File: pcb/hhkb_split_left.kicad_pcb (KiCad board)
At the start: 4 copper layers, 140.4 x 97.4 mm, 67 parts, among them SW1 Esc, SW10 E, SW11 R, SW12 T, SW13 Ctrl, SW14 A, SW15 S, SW16 D, SW17 F, SW18 G, SW19 Shift, SW2 1, SW20 Z, SW21 X, SW22 C, SW23 V, SW24 B, SW25 Alt, SW26 Meta, SW27 L-Space, SW3 2, SW4 3, SW5 4, SW6 5, SW7 Tab, SW8 Q, SW9 W, U1 74HC595

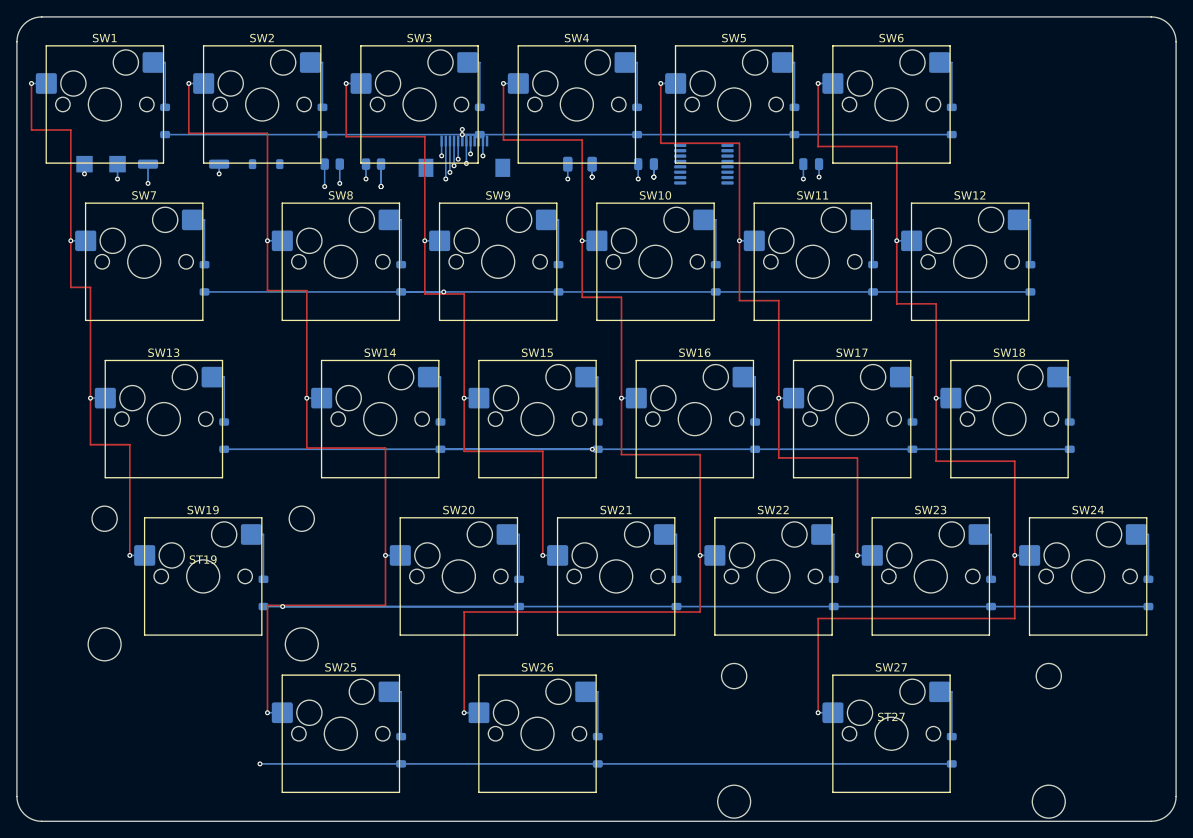
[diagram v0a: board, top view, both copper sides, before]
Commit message: 本体基板の配線が通った（3 基板すべて DRC 違反 0・未配線 0）
Freerouting が詰まっていた原因は 3 つあり、すべて実験で特定した。

1. J_DB（FFC）がダイオード列に載っていた。上段キーのダイオードは帯へ
   1.75mm 食い込み 19.05mm ピッチで並ぶ。帯の部品で J_DB だけ背が高く
   （7.9mm）、その x がちょうど D3 の列だった。短絡・コートヤード重なり・
   ROW0 の未配線はすべてこれが原因。J_DB とその玉突きで C_BULK / C_MCU を
   ダイオードの隙間へ移した

2. GND パッドがベタに届かなかった。GND ベタは In1.Cu の 1 層だけ、GND
   パッドは全部 B.Cu の SMD。間のビアを Freerouting 任せにすると、混んだ
   区画でファンアウトに失敗する（対応 SMD ピンの 42% しか成功しなかった）。
   tools/gnd_fanout.py で配置段階に決定的に立てる

3. ピンが空の (net GND) を DSN に残すと Freerouting が NPE で落ちる。
   GND はネット定義・クラス・plane をまとめて消す。ファンアウトの配線材は
   (type protect) にしてネット無しの固定障害物として渡す（消すと避けない）

ImportSpecctraSES は既存配線を作り直すのでファンアウトが消える
（実測 7 個 → 0 個）。取り込み後に立て直している。

WIP_BOARDS が空になった。DRC の検査が skip ではなく PASS で通る。
検査 249 件通過、組み立て干渉 0。

Co-Authored-By: Claude Opus 5 <noreply@anthropic.com>
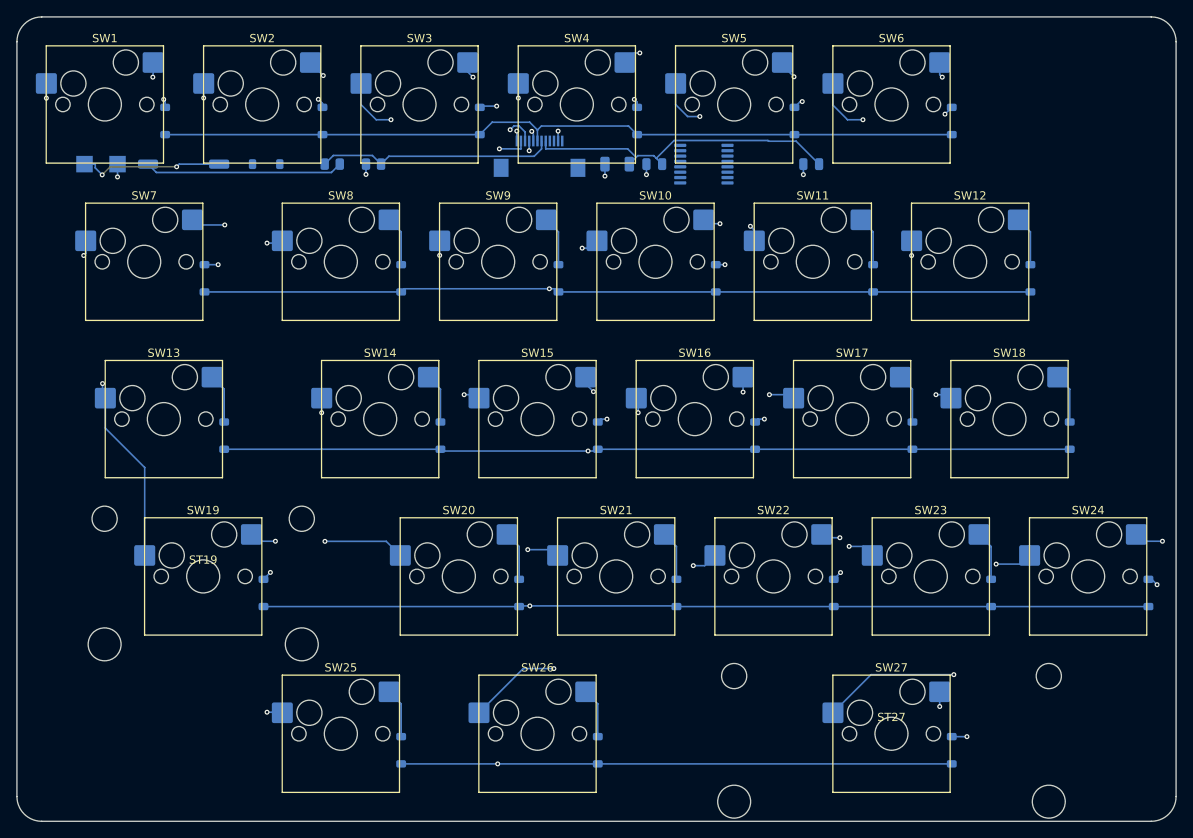
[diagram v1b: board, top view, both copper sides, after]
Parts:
- moved J_DB 9.10 mm to (143.1, 68.2)
- moved C_BULK 4.50 mm to (152.5, 69.1)
- moved C_MCU 1.00 mm to (157.0, 69.1)
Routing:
- net ROW3: track 212.4 -> 173.6 mm
- net V3V3: track 76.8 -> 38.9 mm, vias 6 -> 0
- net ROW2: track 174.9 -> 143.9 mm
- net COL3: track 137.6 -> 107.2 mm
- net ROW4: track 181.7 -> 153.0 mm
- net COL5: track 132.8 -> 107.8 mm
- net COL1: track 123.3 -> 100.6 mm
- net COL2: track 88.2 -> 73.5 mm
- net COL4: track 88.2 -> 73.9 mm
- net COL0: track 76.3 -> 64.0 mm, vias 4 -> 3
- net VBATT_SW: track 36.0 -> 24.1 mm, vias 2 -> 0
- net VBATT_SENSE: track 40.1 -> 28.8 mm, vias 4 -> 0
- net VBATT_RAW: track 27.8 -> 17.6 mm
- net SW7_D: track 6.89 -> 11.0 mm, vias 0 -> 2
- net SW24_D: track 6.89 -> 10.3 mm, vias 0 -> 2
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
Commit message: 手書きルータを削除し、GND 面とファンアウトの検査を足した
gen_pcb.py は配置・ネット・ゾーン・設計規則だけになった（812→501 行）。
_route / _route_electronics / _link / _clear_x / _fcu_verticals /
_nearest_via / _track / _via / _pad / _npth_holes と、レーン関係の定数を削除。

検査を 2 つ追加。どちらも故意に壊して落ちることを確認済み。

- In1.Cu に配線が無いこと（GND 基準面が切られていない）。
  _protect_the_ground_plane を外すと左 38 本・右 65 本が In1 に引かれる。
  **DRC はこれを何も言わない。**分割の 2.4GHz にとって基準面の連続性は
  4 層にした理由そのものなので、ここは機械で守る
- 電子部品の GND パッドの脇にビアがあること。SES 取り込み後の
  再ファンアウトを外すと未配線が左 6・右 7 件出る

配線の質（手書き → Freerouting）:
  総長  左 1817→1574mm / 右 2290→1940mm
  ビア  左 58→68 / 右 68→111
  遠回りの最大  2.3→1.6
  In1.Cu の配線 0 本・GND の島 1 個 は据え置き
  DRC 違反 左 33→0 / 右 32→0

F.Cu は 0 本。信号は In2.Cu と B.Cu で足りている。

Co-Authored-By: Claude Opus 5 <noreply@anthropic.com>
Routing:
- net COL4: track 73.9 -> 103.5 mm
- net COL1: track 100.6 -> 111.0 mm
- net SW23_D: track 6.03 -> 11.5 mm, vias 0 -> 2
- net SW7_D: track 11.0 -> 6.03 mm, vias 2 -> 0
- net ROW1: track 122.9 -> 119.6 mm
- net ROW3: track 173.6 -> 170.7 mm
- net ROW4: track 153.0 -> 155.9 mm
- net COL5: track 107.8 -> 110.6 mm
- net SW21_D: track 6.03 -> 8.41 mm, vias 0 -> 2
- net COL3: track 107.2 -> 109.4 mm
- net VBATT_SENSE: track 28.8 -> 30.7 mm
- net COL0: track 64.0 -> 62.1 mm, vias 3 -> 0
- net SW3_D: track 8.84 -> 6.99 mm
- net SW5_D: track 6.96 -> 8.43 mm
- net SW10_D: track 8.49 -> 7.33 mm
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
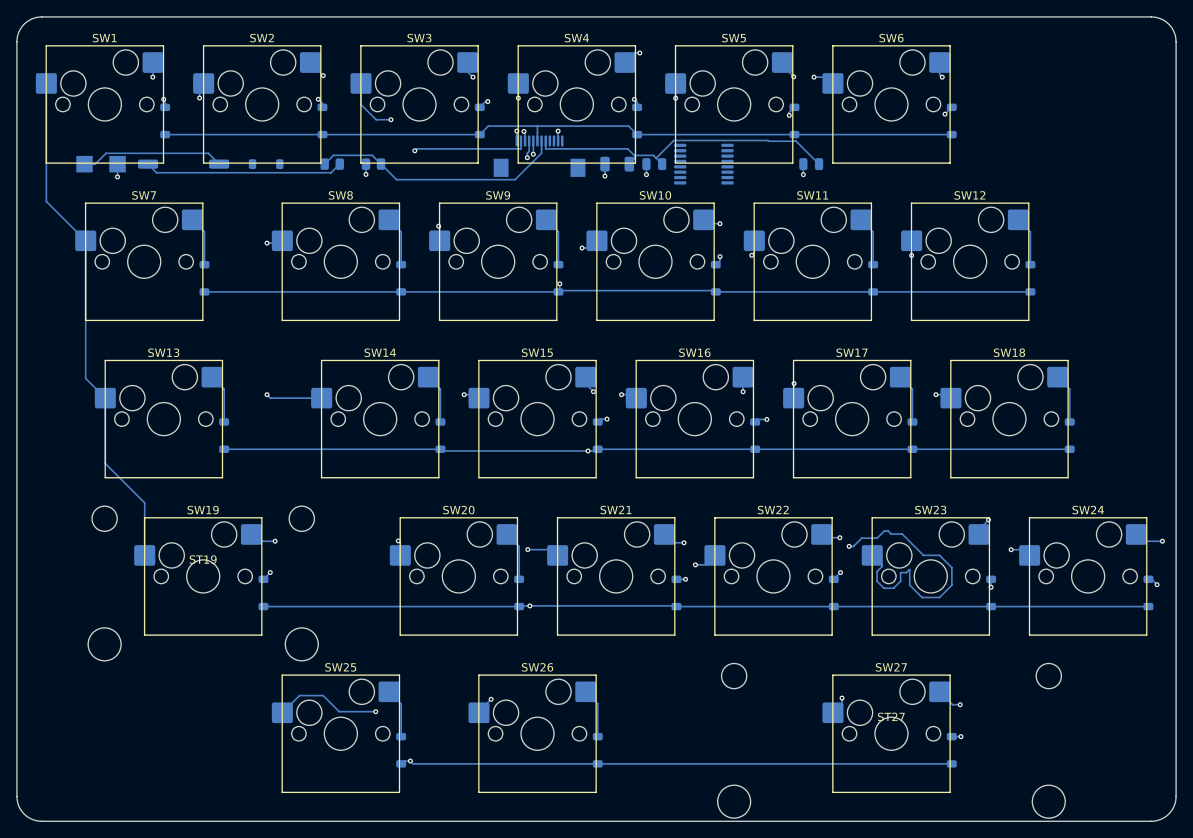
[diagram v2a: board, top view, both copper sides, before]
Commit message: スイッチ→ダイオードを自分で引き、ビアを 4〜5 割減らした
自動配線器が数 mm の接続のために内層へ往復し、SW*_D だけで左 30 個・
右 62 個のビアを使っていた（右が多いのは列のバスが 9 本あって裏面が
混むため）。ソケットの端子とダイオードのアノードは同じ x に並べてあり
（DIODE_OFFSET はそのために選んだ値）、裏面の L 字 2 本で届く。
**経路に選択の余地が無い**ので prewire_switch_diode で自分で引き、
GND と同じく DSN からネットごと外して (type protect) で渡す。

  ビア 左 68→40 / 右 111→51   総長 左 1574→1538 / 右 1940→1902mm
  左右の比 1.28 がキー数の比 1.26 とほぼ一致し、非対称が規模差だけで
  説明できるようになった。DRC は 0/0 のまま

FFC が子基板まで届くかの検査を足した。J_DB を左 9.1mm・右 8.5mm
動かしたのに、それを見る検査が無かった（ケーブルは発注品なので、
合わないと分かるのが組み立て時になる）。左 92.1mm / 右 78.5mm 要り、
100mm で足りる。FFC_LENGTH / FFC_SLACK は暫定値として登録。
左右で同じケーブルが使えることも見る（部品表を 2 種類にしない）。

検査を書く途中で test_pcb.footprints() が信用できないと分かった。
`.*?` で最初の (at ...) を拾うため、J_DB では左が誤った座標・右が空を
返す。この検査では括弧の対応で切り出す _footprint_blocks を使った。

Co-Authored-By: Claude Opus 5 <noreply@anthropic.com>
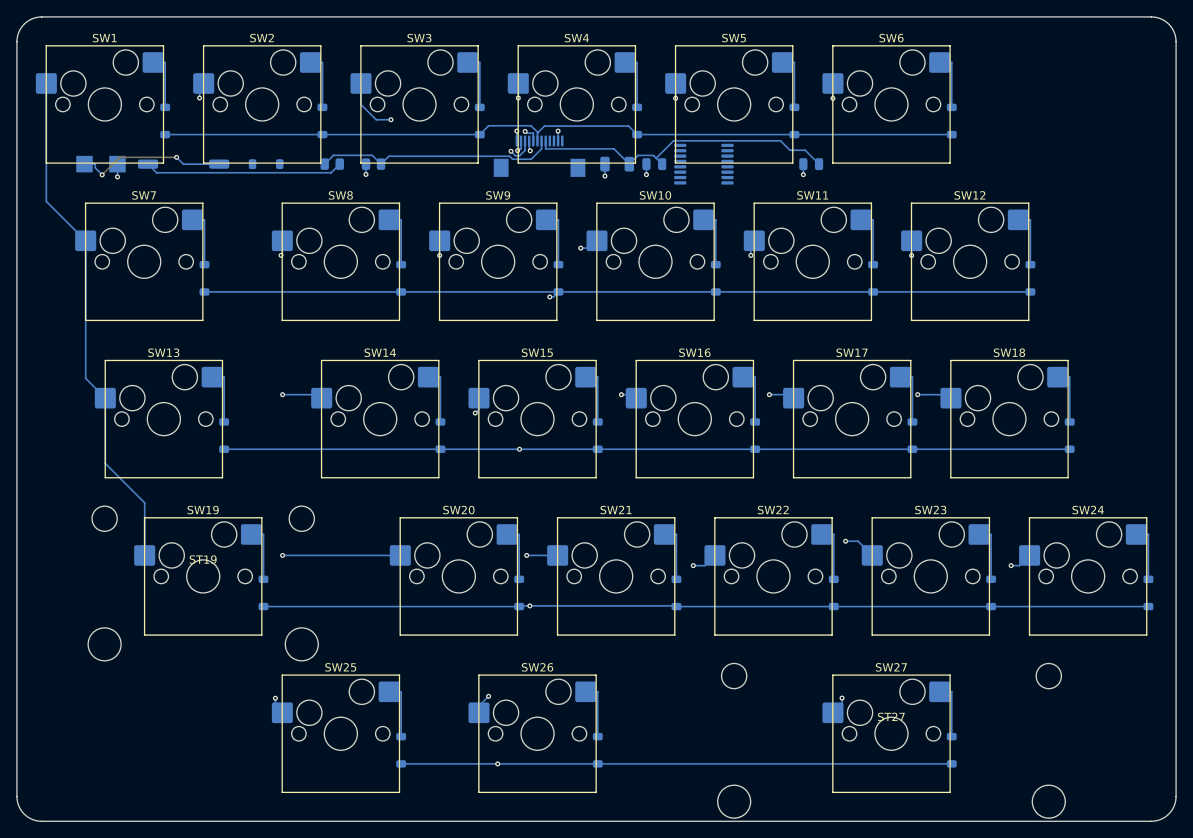
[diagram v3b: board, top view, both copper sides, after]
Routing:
- net COL4: track 103.5 -> 72.9 mm
- net COL5: track 110.6 -> 119.6 mm
- net COL1: track 111.0 -> 102.3 mm
- net ROW1: track 119.6 -> 124.9 mm
- net SW23_D: track 11.5 -> 6.89 mm, vias 2 -> 0
- net ROW4: track 155.9 -> 152.2 mm
- net SW24_D: track 10.3 -> 6.89 mm, vias 2 -> 0
- net SW4_D: track 9.26 -> 6.89 mm, vias 2 -> 0
- net ROW3: track 170.7 -> 172.4 mm
- net VBATT_SENSE: track 30.7 -> 29.2 mm
- net SW5_D: track 8.43 -> 6.89 mm, vias 2 -> 0
- net SW21_D: track 8.41 -> 6.89 mm, vias 2 -> 0
- net SW19_D: track 8.40 -> 6.89 mm, vias 2 -> 0
- net ROW2: track 144.6 -> 146.0 mm
- net SW27_D: track 8.15 -> 6.89 mm, vias 2 -> 0
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
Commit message: 電源スイッチを基板から外し、背面パネルへ（open-gaps #17 解決）
基板の後端からケース背面まで 23.3mm あり、基板の上のどこに置いても
背面には出せない。「基板に載せる」という前提自体が誤りだった。

SW_PWR の種類を wire_pads にし、基板は SW_PWR_1 / SW_PWR_2 の
ランド 2 個で受ける。電池ボックスと同じ形。実物は背面パネルに付けて
配線で繋ぐ。部品はプッシュロック（オルタネート）の丸ボタン
（実機の「電源／Bluetooth ペアリング」も丸ボタン。機械接点なので
電池を本当に切り離せる）。

再発防止に test_no_user_operated_part_is_sealed_inside を追加。
故意にスイッチを基板へ戻すと落ちることを確認済み。**最初に書いた版は
空振りしていた**（配線済み基板を読むのに再生成しか走らせておらず、
検査対象が変わっていなかった）。配線まで通して確かめ直した。

ランド 2 個への展開規則を circuit.board_refs に一本化した。
gen_pcb と test_pcb と test_conformance が別々に「battery_holder だけ
2 個」と持っていたため、電源スイッチを変えた瞬間に検査 6 件が落ちた。

検査 260 件通過。DRC は 3 基板とも 0/0 のまま。

Co-Authored-By: Claude Opus 5 <noreply@anthropic.com>
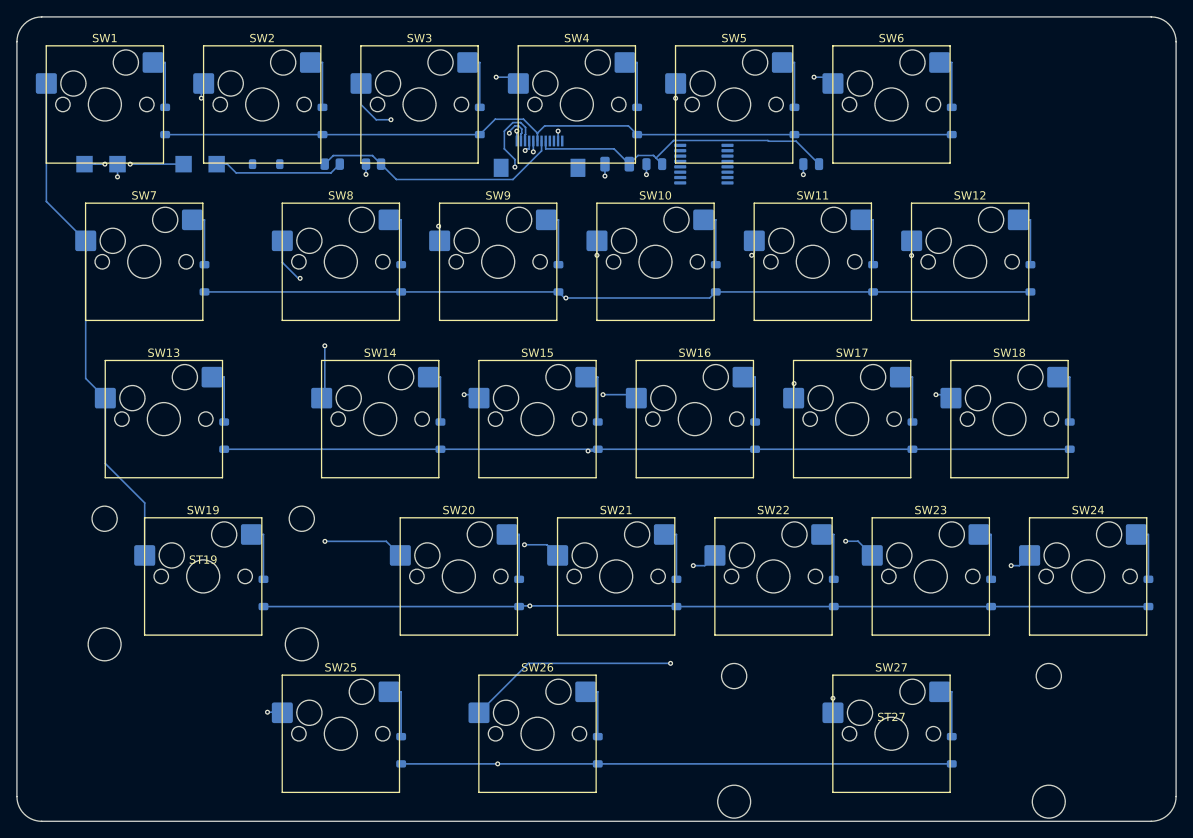
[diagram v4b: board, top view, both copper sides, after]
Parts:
- removed SW_PWR: slide_switch, SW_DIP_SPSTx01_Slide_9.78x4.72mm_W8.61mm_P2.54mm
- added SW_PWR_1: wire_pads, TestPoint_Pad_2.0x2.0mm, B.Cu at (100.0, 69.1)
- added SW_PWR_2: wire_pads, TestPoint_Pad_2.0x2.0mm, B.Cu at (104.0, 69.1)
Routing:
- net COL3: track 108.3 -> 119.8 mm
- net COL5: track 119.6 -> 110.1 mm
- net VBATT_SW: track 24.1 -> 15.8 mm
- net COL1: track 102.3 -> 109.2 mm
- net VBATT_RAW: track 18.3 -> 12.0 mm
- net ROW1: track 124.9 -> 121.3 mm
- net ROW4: track 152.2 -> 155.4 mm
- net ROW3: track 172.4 -> 175.3 mm
- net COL4: track 72.9 -> 71.6 mm
- net VBATT_SENSE: track 29.2 -> 30.5 mm
- net ROW0: track 97.8 -> 98.5 mm
- net COL2: track 74.0 -> 73.5 mm

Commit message: 電源スイッチの決定を記録し、追随できていなかった 3 箇所を直した
decisions/2026-08-08-power-switch.md を追加。基板に載せない理由
（後端から背面まで 23.3mm）、丸ボタンでなくスライドにした理由
（左の枠が幅 10.6mm しかなく、直径がそのまま幅を食う丸型は不利）、
覆す前に読むことを残した。

**変更に追随できていなかった箇所を 3 つ見つけて直した:**

1. test_resources.py の部品表が古かった。595 が SOIC-16（7.4x10.4）の
   ままで、基板から外した「スライドスイッチ 9.0x5.0」も残っていた。
   TSSOP-16（7.79x5.59）と「電源スイッチのランド 4.0x4.0 x2」へ。
   この表は「書き漏らすと誰も気づかない」ためのものなので、古いままだと
   目的を果たさない
2. gen_pcb.py の嘘コメント 2 つ（「手前の帯に電源。手が届く側に置く」
   「スライドスイッチは 9.78x4.72mm。帯に収まる」）
3. gnd_fanout.py の ELEC 正規表現が SW_PWR 止まりで SW_PWR_1 を拾えない

3 は test_pcb.py の ELEC_REF と同じ式の二重管理だった。circuit.py へ
一本化した（board_refs / WIRE_PAD_KINDS と同じ理由）。

実機との差を open-gaps #20 に記録（形式・機能・位置）。

検査 262 件通過。DRC は 3 基板とも 0/0。

Co-Authored-By: Claude Opus 5 <noreply@anthropic.com>
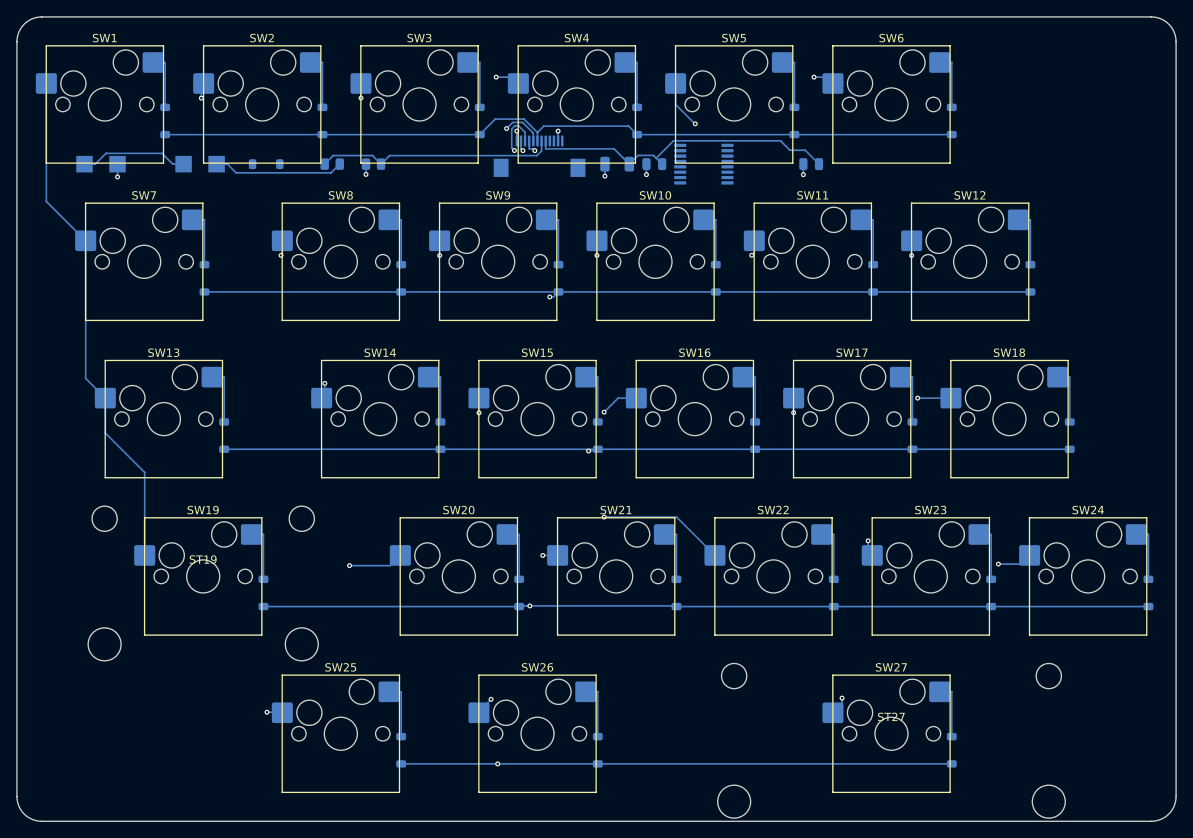
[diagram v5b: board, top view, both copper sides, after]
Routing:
- net COL1: track 109.2 -> 100.1 mm
- net ROW1: track 121.3 -> 129.1 mm
- net COL3: track 119.8 -> 113.8 mm
- net ROW4: track 155.4 -> 150.5 mm
- net COL2: track 73.5 -> 71.6 mm
- net COL5: track 110.1 -> 111.9 mm
- net ROW3: track 175.3 -> 173.6 mm
- net VBATT_SENSE: track 30.5 -> 29.0 mm
- net VBATT_RAW: track 12.0 -> 13.1 mm, vias 2 -> 0
- net ROW2: track 145.6 -> 144.7 mm
- net COL4: track 71.6 -> 70.7 mm

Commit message: 1 回発注に合わせ、アンテナで無料でできることを全部やった
発注を 1 回にまとめると決めたので、**発注前に測る手段が無くなった。**
そこで方針を「測るまで止める」から「無料の対策を全部やる＋手戻りを
子基板 1 枚に閉じ込める」へ変えた。

**新たに 3 つの案を数字で潰した**（open-gaps #23 の表に追記）:
- 子基板の銅を抜く … アンテナの影 3mm のうち 2mm が FFC コネクタの下
- 90° 回す（再検討）… 左はアンテナと電池が -0.6mm（必要 10mm）
- 右の子基板を空いた x へ … どこに置いても最良で 9 本掛かる

**やったこと: 本体基板の禁止域（左のみ）。**
一度「支配的でない」として捨てた案を入れ直した。無料だから。
左は 30x15mm を全層で禁止域にでき、配線を 1 本も動かさずに入った
（DRC 0 のまま。ビア +1・配線 +4mm）。右は列のバス 9 本が横断していて
入らない。**Freerouting 2.3.0 は DSN の禁止域を守らない**（4 層とも
正しく出ていることは確認）。左が通ったのは偶然そこを使わなかっただけ。

効き目は限定的なはず。波長 125mm に対して窓が小さい。
**「やらないよりまし」以上の主張はしない。**

手戻りの封じ込め:
- test_the_cable_interface_is_frozen が FFC の界面を凍結。子基板を
  作り直しても本体基板 2 枚とケーブルは無傷
- 止め具を「承知の記録が無いまま製造ファイルを出すな」へ書き換えた
  （子基板だけ先に出す前提が消えたため）

**設定しただけでは効いていない**ので 2 つ検査を足した:
- test_the_antenna_keepout_is_actually_empty（実基板に銅が無いこと）
- test_the_antenna_keepout_covers_the_real_antenna（ケース側と位置照合）
どちらも故意にずらして落ちることを確認した。

autoroute.py の java 選びも直した。macOS の /usr/bin/java は存在するが
実行すると失敗するスタブで、存在検査だけだとこれを選んで**配線が黙って
失敗する**（実際に起きた）。-version が通ることまで見る。

3 基板とも DRC 0 / 未配線 0。組み立て干渉 0。検査 282 件。

Co-Authored-By: Claude Opus 5 (1M context) <noreply@anthropic.com>
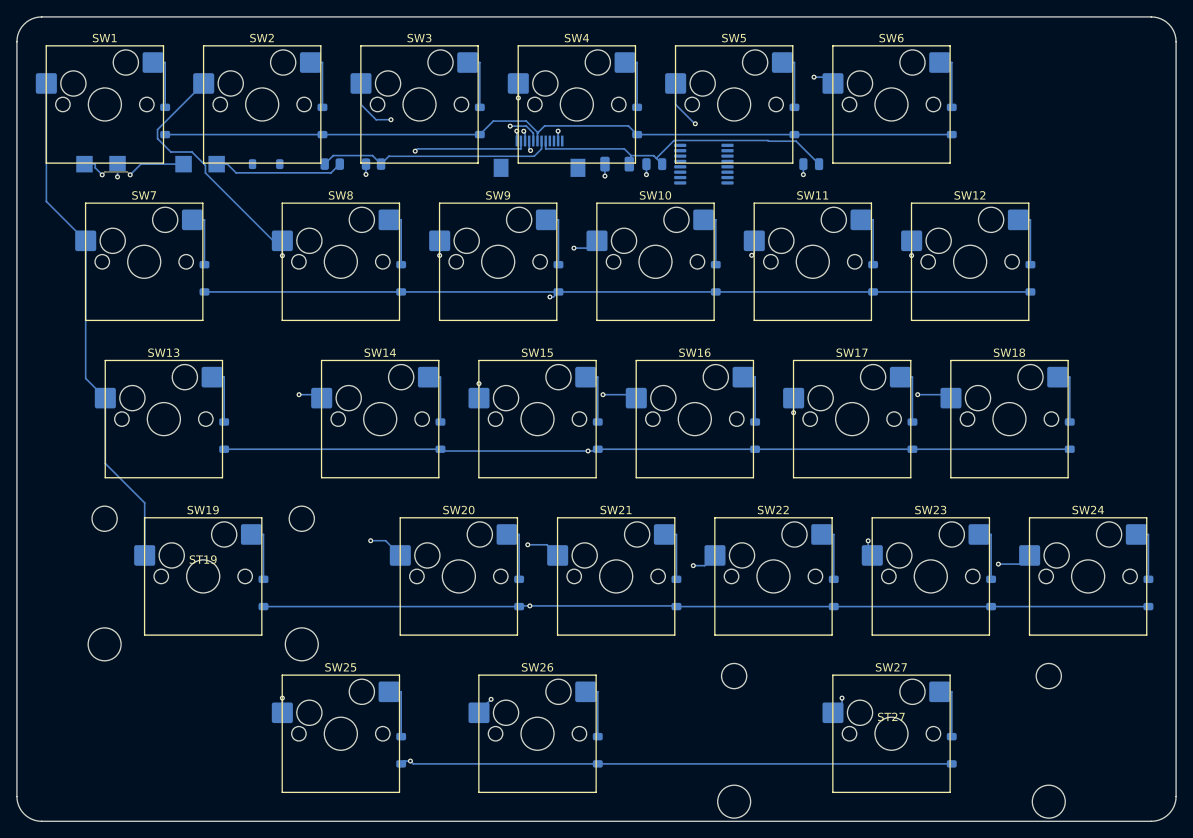
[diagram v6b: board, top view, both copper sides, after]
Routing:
- net ROW4: track 150.5 -> 155.8 mm
- net COL1: track 100.1 -> 103.0 mm, vias 5 -> 4
- net ROW3: track 173.6 -> 170.9 mm
- net COL3: track 113.8 -> 111.2 mm
- net COL2: track 71.6 -> 73.0 mm
- net ROW1: track 129.1 -> 128.3 mm
- net VBATT_RAW: track 13.1 -> 13.6 mm, vias 0 -> 2
